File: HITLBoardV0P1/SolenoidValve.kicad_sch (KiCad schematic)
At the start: 10 parts, among them Q1 NPN, Q2 PMOS

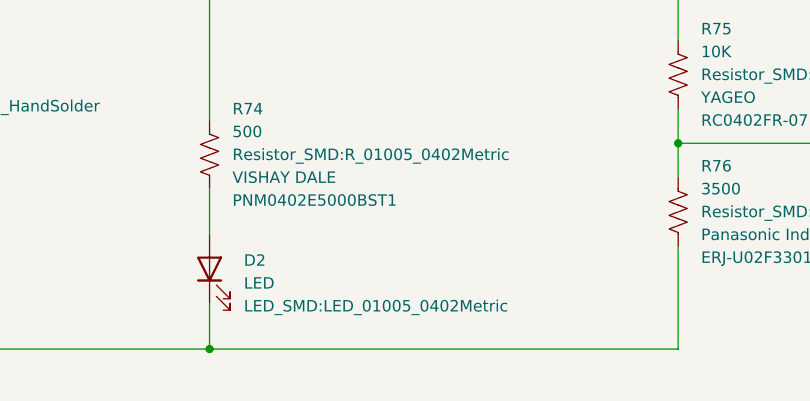
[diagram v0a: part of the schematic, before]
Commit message: add debug LEDs and reset_n button for system reset
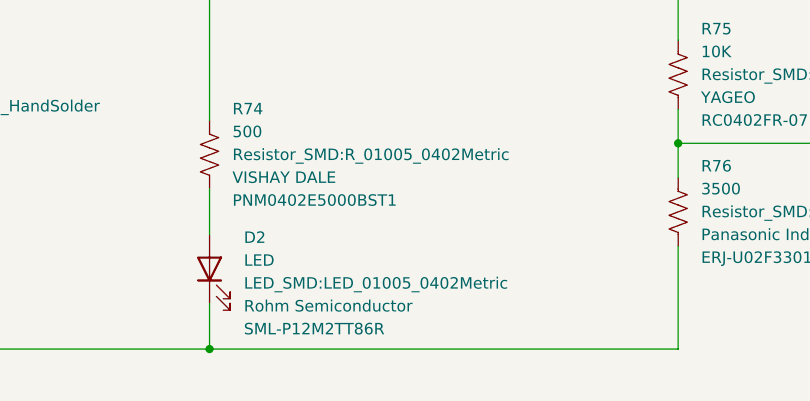
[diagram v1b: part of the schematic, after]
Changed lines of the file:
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@@
 		(fields_autoplaced yes)
 		(property "Reference" "D2"
+			(at 223.52 82.8674 90)
+			(show_name no)
+			(do_not_autoplace no)
+			(effects
+				(font
+					(size 1.27 1.27)
+				)
+				(justify right)
+			)
+		)
+		(property "Value" "LED"
 			(at 223.52 85.4074 90)
 			(show_name no)
@@
 			)
 		)
-		(property "Value" "LED"
+		(property "Footprint" "LED_SMD:LED_01005_0402Metric"
 			(at 223.52 87.9474 90)
-			(show_name no)
-			(do_not_autoplace no)
-			(effects
-				(font
-					(size 1.27 1.27)
-				)
-				(justify right)
-			)
-		)
-		(property "Footprint" "LED_SMD:LED_01005_0402Metric"
-			(at 223.52 90.4874 90)
 			(show_name no)
 			(do_not_autoplace no)
@@
 		)
 		(property "MFG" "Rohm Semiconductor"
-			(at 219.71 86.36 90)
-			(hide yes)
+			(at 223.52 90.4874 90)
 			(show_name no)
 			(do_not_autoplace no)
@@
 					(size 1.27 1.27)
 				)
+				(justify right)
 			)
 		)
 		(property "MPN" "SML-P12M2TT86R"
-			(at 219.71 86.36 90)
-			(hide yes)
+			(at 223.52 93.0274 90)
 			(show_name no)
 			(do_not_autoplace no)
@@
 					(size 1.27 1.27)
 				)
+				(justify right)
 			)
 		)
